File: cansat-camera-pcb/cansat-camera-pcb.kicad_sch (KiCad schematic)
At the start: 19 parts, among them SW2 SW_Push, U4 STM32H743ZITx, Y1 25MHz

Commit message: -
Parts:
- U4: footprint Package_QFP:LQFP-144_20x20mm_P0.5mm -> (none)
- Y1: value 25MHz -> 24MHz
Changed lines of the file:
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@@
 			)
 		)
-		(property "Footprint" "Package_QFP:LQFP-144_20x20mm_P0.5mm"
+		(property "Footprint" ""
 			(at 62.23 242.57 0)
 			(effects
@@
 			)
 		)
-		(property "Value" "25MHz"
+		(property "Value" "24MHz"
 			(at 46.99 92.7099 90)
 			(effects

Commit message: Footprint assign
Reset kivételével minden hozzácsatolva
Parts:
- C1, C10, C11, C12, C2, C3, C34, C4, C8, C9, R1, R14, R2: footprint (none) -> Capacitor_SMD:C_0402_1005Metric
- C13, C35, C36: footprint (none) -> Capacitor_SMD:C_0201_0603Metric
- U4: footprint (none) -> Package_QFP:LQFP-144_20x20mm_P0.5mm
- Y1: footprint (none) -> Crystal:Crystal_SMD_HC49-SD_HandSoldering
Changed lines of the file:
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@@
 			)
 		)
-		(property "Footprint" ""
+		(property "Footprint" "Capacitor_SMD:C_0402_1005Metric"
 			(at 85.09 36.83 0)
 			(effects
@@
 			)
 		)
-		(property "Footprint" ""
+		(property "Footprint" "Capacitor_SMD:C_0402_1005Metric"
 			(at 49.53 60.96 0)
 			(effects
@@
 			)
 		)
-		(property "Footprint" ""
+		(property "Footprint" "Capacitor_SMD:C_0402_1005Metric"
 			(at 83.82 262.89 0)
 			(effects
@@
 			)
 		)
-		(property "Footprint" ""
+		(property "Footprint" "Capacitor_SMD:C_0402_1005Metric"
 			(at 104.14 262.89 0)
 			(effects
@@
 			)
 		)
-		(property "Footprint" ""
+		(property "Footprint" "Package_QFP:LQFP-144_20x20mm_P0.5mm"
 			(at 62.23 242.57 0)
 			(effects
@@
 			)
 		)
-		(property "Footprint" ""
+		(property "Footprint" "Capacitor_SMD:C_0201_0603Metric"
 			(at 43.18 226.06 0)
 			(effects
@@
 			)
 		)
-		(property "Footprint" ""
+		(property "Footprint" "Capacitor_SMD:C_0402_1005Metric"
 			(at 46.99 74.93 0)
 			(effects
@@
 			)
 		)
-		(property "Footprint" ""
+		(property "Footprint" "Capacitor_SMD:C_0402_1005Metric"
 			(at 39.37 87.63 0)
 			(effects
@@
 			)
 		)
-		(property "Footprint" ""
+		(property "Footprint" "Capacitor_SMD:C_0402_1005Metric"
 			(at 77.47 33.02 0)
 			(effects
@@
 			)
 		)
-		(property "Footprint" ""
+		(property "Footprint" "Crystal:Crystal_SMD_HC49-SD_HandSoldering"
 			(at 44.45 91.44 0)
 			(effects
@@
 			)
 		)
-		(property "Footprint" ""
+		(property "Footprint" "Capacitor_SMD:C_0402_1005Metric"
 			(at 73.66 262.89 0)
 			(effects
@@
 			)
 		)
-		(property "Footprint" ""
+		(property "Footprint" "Capacitor_SMD:C_0201_0603Metric"
 			(at 114.3 262.89 0)
 			(effects
@@
 			)
 		)
-		(property "Footprint" ""
+		(property "Footprint" "Capacitor_SMD:C_0402_1005Metric"
 			(at 39.37 95.25 0)
 			(effects
@@
 			)
 		)
-		(property "Footprint" ""
+		(property "Footprint" "Capacitor_SMD:C_0402_1005Metric"
 			(at 100.33 36.83 0)
 			(effects
@@
 			)
 		)
-		(property "Footprint" ""
+		(property "Footprint" "Capacitor_SMD:C_0402_1005Metric"
 			(at 93.98 262.89 0)
 			(effects
@@
 			)
 		)
-		(property "Footprint" ""
+		(property "Footprint" "Capacitor_SMD:C_0201_0603Metric"
 			(at 43.18 231.14 0)
 			(effects
@@
 			)
 		)
-		(property "Footprint" ""
+		(property "Footprint" "Capacitor_SMD:C_0402_1005Metric"
 			(at 63.5 262.89 0)
 			(effects
@@
 			)
 		)
-		(property "Footprint" ""
+		(property "Footprint" "Capacitor_SMD:C_0402_1005Metric"
 			(at 92.71 33.02 0)
 			(effects

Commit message: button footprint added to library and assigned
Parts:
- SW2: footprint (none) -> gaia-camera-footprints:KEY-SMD_L4.0-W3.0-LS4.9-1
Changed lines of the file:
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@@
 			)
 		)
-		(property "Footprint" ""
+		(property "Footprint" "gaia-camera-footprints:KEY-SMD_L4.0-W3.0-LS4.9-1"
 			(at 41.91 62.23 0)
 			(effects

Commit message: Footprint assign final
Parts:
- C13, C35, C36: footprint Capacitor_SMD:C_0201_0603Metric -> Capacitor_SMD:C_0603_1608Metric
- Y1: footprint Crystal:Crystal_SMD_HC49-SD_HandSoldering -> Crystal:Crystal_SMD_HC49-SD
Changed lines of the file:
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@@
 			)
 		)
-		(property "Footprint" "Capacitor_SMD:C_0201_0603Metric"
+		(property "Footprint" "Capacitor_SMD:C_0603_1608Metric"
 			(at 43.18 226.06 0)
 			(effects
@@
 			)
 		)
-		(property "Footprint" "Crystal:Crystal_SMD_HC49-SD_HandSoldering"
+		(property "Footprint" "Crystal:Crystal_SMD_HC49-SD"
 			(at 44.45 91.44 0)
 			(effects
@@
 			)
 		)
-		(property "Footprint" "Capacitor_SMD:C_0201_0603Metric"
+		(property "Footprint" "Capacitor_SMD:C_0603_1608Metric"
 			(at 114.3 262.89 0)
 			(effects
@@
 			)
 		)
-		(property "Footprint" "Capacitor_SMD:C_0201_0603Metric"
+		(property "Footprint" "Capacitor_SMD:C_0603_1608Metric"
 			(at 43.18 231.14 0)
 			(effects

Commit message: Alkatrész elhelyezés final
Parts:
- Y1: footprint Crystal:Crystal_SMD_HC49-SD -> Crystal:Crystal_SMD_3225-4Pin_3.2x2.5mm
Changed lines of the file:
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@@
 			)
 		)
-		(property "Footprint" "Crystal:Crystal_SMD_HC49-SD"
+		(property "Footprint" "Crystal:Crystal_SMD_3225-4Pin_3.2x2.5mm"
 			(at 44.45 91.44 0)
 			(effects

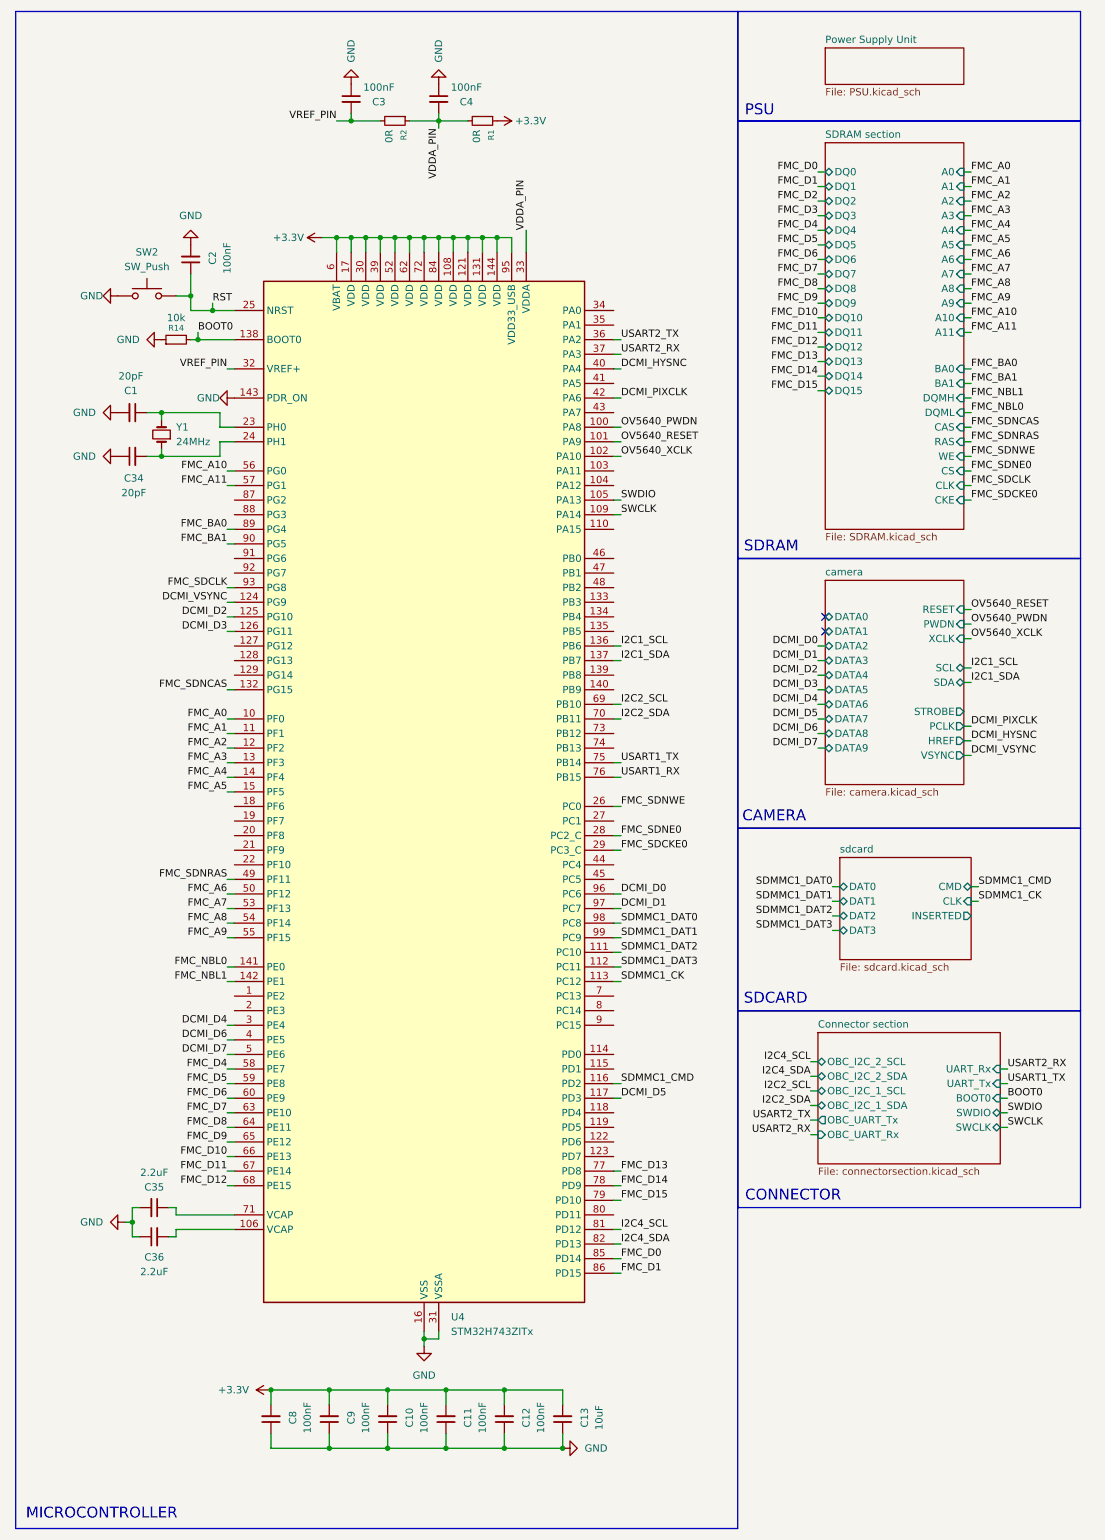
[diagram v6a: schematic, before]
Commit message: Routing+SDram csere
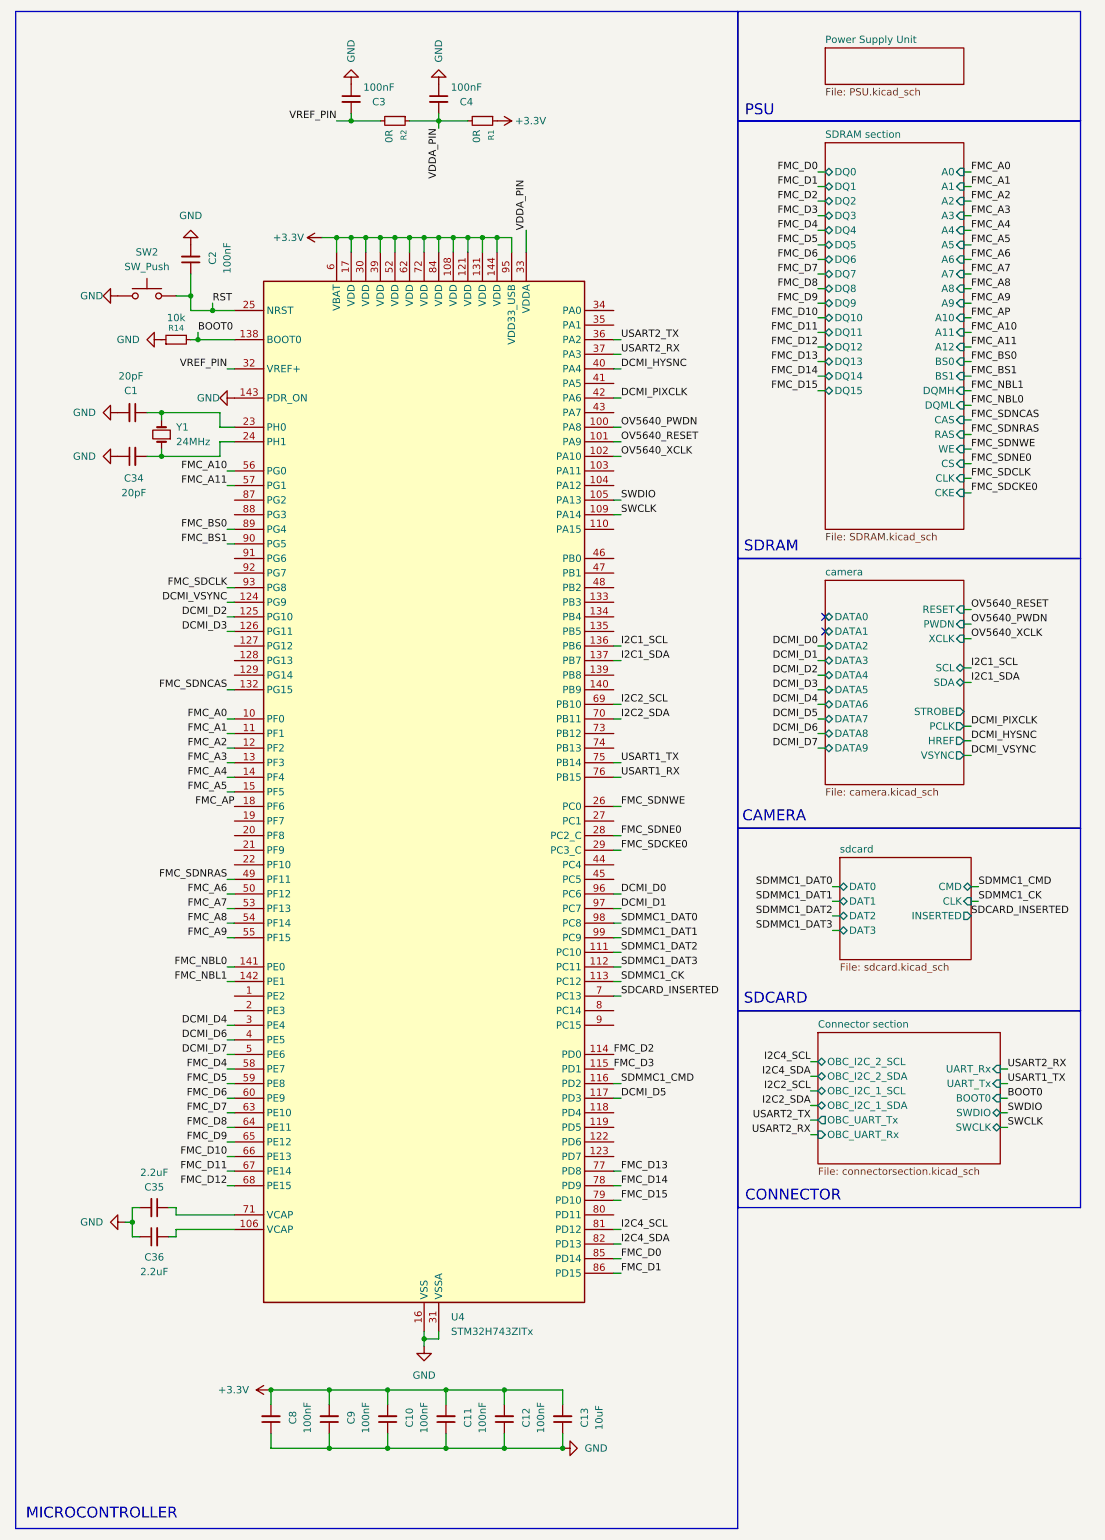
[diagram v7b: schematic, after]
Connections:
- net FMC_D2: now also U4.114 (PD0)
- net FMC_D3: now also U4.115 (PD1)
- net FMC_AP: now reaches U4.18 (PF6)
- net SDCARD_INSERTED: now reaches U4.7 (PC13)
- net FMC_BA0 renamed FMC_BS0
- net FMC_BA1 renamed FMC_BS1
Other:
- sheet SDRAM section ports: added A12, BS0, BS1; removed BA0, BA1
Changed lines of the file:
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@@
 	(wire
 		(pts
-			(xy 184.15 102.87) (xy 185.42 102.87)
+			(xy 184.15 101.6) (xy 185.42 101.6)
 		)
 		(stroke
@@
 	(wire
 		(pts
-			(xy 184.15 95.25) (xy 185.42 95.25)
+			(xy 184.15 93.98) (xy 185.42 93.98)
 		)
 		(stroke
@@
 	(wire
 		(pts
-			(xy 184.15 80.01) (xy 185.42 80.01)
+			(xy 184.15 78.74) (xy 185.42 78.74)
 		)
 		(stroke
@@
 	(wire
 		(pts
-			(xy 184.15 85.09) (xy 185.42 85.09)
+			(xy 184.15 83.82) (xy 185.42 83.82)
 		)
 		(stroke
@@
 	(wire
 		(pts
+			(xy 184.15 76.2) (xy 185.42 76.2)
+		)
+		(stroke
+			(width 0)
+			(type default)
+		)
+	)
+	(wire
+		(pts
 			(xy 185.42 170.18) (xy 186.69 170.18)
 		)
@@
 	(wire
 		(pts
-			(xy 184.15 92.71) (xy 185.42 92.71)
+			(xy 184.15 91.44) (xy 185.42 91.44)
 		)
 		(stroke
@@
 	(wire
 		(pts
-			(xy 184.15 90.17) (xy 185.42 90.17)
+			(xy 184.15 88.9) (xy 185.42 88.9)
 		)
 		(stroke
@@
 	(wire
 		(pts
-			(xy 184.15 100.33) (xy 185.42 100.33)
+			(xy 184.15 99.06) (xy 185.42 99.06)
 		)
 		(stroke
@@
 	(wire
 		(pts
-			(xy 184.15 82.55) (xy 185.42 82.55)
+			(xy 184.15 81.28) (xy 185.42 81.28)
 		)
 		(stroke
@@
 	(wire
 		(pts
+			(xy 124.46 189.23) (xy 123.19 189.23)
+		)
+		(stroke
+			(width 0)
+			(type default)
+		)
+	)
+	(wire
+		(pts
 			(xy 87.63 57.15) (xy 90.17 57.15)
 		)
@@
 	(wire
 		(pts
-			(xy 184.15 97.79) (xy 185.42 97.79)
+			(xy 184.15 96.52) (xy 185.42 96.52)
 		)
 		(stroke
@@
 	(wire
 		(pts
-			(xy 184.15 87.63) (xy 185.42 87.63)
+			(xy 184.15 86.36) (xy 185.42 86.36)
 		)
 		(stroke
@@
 		)
 	)
-	(label "FMC_BA1"
-		(at 185.42 82.55 0)
+	(label "FMC_BS1"
+		(at 185.42 81.28 0)
 		(effects
 			(font
@@
 	)
 	(label "FMC_SDNRAS"
-		(at 185.42 92.71 0)
+		(at 185.42 91.44 0)
 		(effects
 			(font
@@
 		)
 	)
-	(label "FMC_BA1"
+	(label "FMC_BS1"
 		(at 55.88 110.49 180)
 		(effects
@@
 		)
 	)
+	(label "SDCARD_INSERTED"
+		(at 185.42 175.26 0)
+		(effects
+			(font
+				(size 1.27 1.27)
+			)
+			(justify left bottom)
+		)
+	)
 	(label "OV5640_PWDN"
 		(at 124.46 90.17 0)
@@
 	)
 	(label "FMC_SDNE0"
-		(at 185.42 97.79 0)
+		(at 185.42 96.52 0)
 		(effects
 			(font
@@
 	)
 	(label "FMC_SDCKE0"
-		(at 185.42 102.87 0)
+		(at 185.42 101.6 0)
 		(effects
 			(font
@@
 		)
 	)
-	(label "FMC_A11"
+	(label "FMC_A10"
 		(at 185.42 73.66 0)
 		(effects
@@
 	)
 	(label "FMC_SDNCAS"
-		(at 185.42 90.17 0)
+		(at 185.42 88.9 0)
 		(effects
 			(font
@@
 		)
 	)
+	(label "SDCARD_INSERTED"
+		(at 124.46 189.23 0)
+		(effects
+			(font
+				(size 1.27 1.27)
+			)
+			(justify left bottom)
+		)
+	)
 	(label "DCMI_VSYNC"
 		(at 185.42 147.32 0)
@@
 	)
 	(label "FMC_SDNWE"
-		(at 185.42 95.25 0)
+		(at 185.42 93.98 0)
 		(effects
 			(font
@@
 		)
 	)
+	(label "FMC_D3"
+		(at 123.19 201.93 0)
+		(effects
+			(font
+				(size 1.27 1.27)
+			)
+			(justify left bottom)
+		)
+	)
 	(label "DCMI_D4"
 		(at 55.88 194.31 180)
@@
 		)
 	)
-	(label "FMC_BA0"
-		(at 185.42 80.01 0)
+	(label "FMC_BS0"
+		(at 185.42 78.74 0)
 		(effects
 			(font
@@
 		)
 	)
-	(label "FMC_A10"
+	(label "FMC_AP"
 		(at 185.42 71.12 0)
 		(effects
@@
 		)
 	)
+	(label "FMC_A11"
+		(at 185.42 76.2 0)
+		(effects
+			(font
+				(size 1.27 1.27)
+			)
+			(justify left bottom)
+		)
+	)
 	(label "VDDA_PIN"
 		(at 92.71 38.1 270)
@@
 		)
 	)
-	(label "FMC_BA0"
+	(label "FMC_BS0"
 		(at 55.88 107.95 180)
 		(effects
@@
 		)
 	)
+	(label "FMC_AP"
+		(at 57.15 156.21 180)
+		(effects
+			(font
+				(size 1.27 1.27)
+			)
+			(justify right bottom)
+		)
+	)
 	(label "FMC_SDCLK"
 		(at 55.88 118.11 180)
@@
 	)
 	(label "FMC_NBL0"
-		(at 185.42 87.63 0)
+		(at 185.42 86.36 0)
 		(effects
 			(font
@@
 		)
 	)
+	(label "FMC_D2"
+		(at 123.19 199.39 0)
+		(effects
+			(font
+				(size 1.27 1.27)
+			)
+			(justify left bottom)
+		)
+	)
 	(label "FMC_NBL1"
-		(at 185.42 85.09 0)
+		(at 185.42 83.82 0)
 		(effects
 			(font
@@
 	)
 	(label "FMC_SDCLK"
-		(at 185.42 100.33 0)
+		(at 185.42 99.06 0)
 		(effects
 			(font
@@
 		)
 		(pin "DQML" input
-			(at 184.15 87.63 0)
+			(at 184.15 86.36 0)
 			(effects
 				(font
@@
 		)
 		(pin "WE" input
-			(at 184.15 95.25 0)
-			(effects
-				(font
-					(size 1.27 1.27)
-				)
-				(justify right)
-			)
-		)
-		(pin "BA0" input
-			(at 184.15 80.01 0)
+			(at 184.15 93.98 0)
 			(effects
 				(font
@@
 		)
 		(pin "CS" input
-			(at 184.15 97.79 0)
-			(effects
-				(font
-					(size 1.27 1.27)
-				)
-				(justify right)
-			)
-		)
-		(pin "BA1" input
-			(at 184.15 82.55 0)
+			(at 184.15 96.52 0)
 			(effects
 				(font
@@
 		)
 		(pin "CAS" input
-			(at 184.15 90.17 0)
+			(at 184.15 88.9 0)
 			(effects
 				(font
@@
 		)
 		(pin "RAS" input
-			(at 184.15 92.71 0)
+			(at 184.15 91.44 0)
 			(effects
 				(font
@@
 		)
 		(pin "DQMH" input
-			(at 184.15 85.09 0)
+			(at 184.15 83.82 0)
 			(effects
 				(font
@@
 		)
 		(pin "CKE" input
-			(at 184.15 102.87 0)
+			(at 184.15 101.6 0)
 			(effects
 				(font
@@
 		)
 		(pin "CLK" input
-			(at 184.15 100.33 0)
+			(at 184.15 99.06 0)
 			(effects
 				(font
@@
 			)
 		)
+		(pin "A12" input
+			(at 184.15 76.2 0)
+			(effects
+				(font
+					(size 1.27 1.27)
+				)
+				(justify right)
+			)
+		)
+		(pin "BS0" input
+			(at 184.15 78.74 0)
+			(effects
+				(font
+					(size 1.27 1.27)
+				)
+				(justify right)
+			)
+		)
+		(pin "BS1" input
+			(at 184.15 81.28 0)
+			(effects
+				(font
+					(size 1.27 1.27)
+				)
+				(justify right)
+			)
+		)

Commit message: ready
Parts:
- added C18, C19, C20, C21, C22, C7: 100nF, Capacitor_SMD:C_0402_1005Metric, symbol Device:C_Small
- R1, R14, R2: footprint Capacitor_SMD:C_0402_1005Metric -> Resistor_SMD:R_0402_1005Metric
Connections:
- net +3.3V: now also C18.2, C19.2, C20.2, C21.2, C22.2, C7.2
- net GND: now also C18.1, C19.1, C20.1, C21.1, C22.1, C7.1
- net UART4_RX: now reaches U4.103 (PA11)
- net UART4_TX: now reaches U4.104 (PA12)
- net I2C2_SCL: no longer names the net of U4.69 (PB10)
- net I2C2_SDA: no longer names the net of U4.70 (PB11)
- net I2C4_SCL: no longer names the net of U4.81 (PD12)
- net I2C4_SDA: no longer names the net of U4.82 (PD13)
- net USART1_RX: no longer names the net of U4.76 (PB15)
- net USART1_TX: no longer names the net of U4.75 (PB14)
- no-connect marks 2 -> 45
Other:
- sheet Connector section ports: added none; removed OBC_I2C_1_SCL, OBC_I2C_1_SDA, OBC_I2C_2_SCL, OBC_I2C_2_SDA, UART_Rx, UART_Tx
- moved on the sheet: C10, C11, C12, C13, C9
